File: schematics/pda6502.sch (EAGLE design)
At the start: 33 parts, among them IC1 74HC00D, IC2 74HC138D, IC3 DS1813-SMD, J1 CON_HEADER_2X07-PTH, J2 CON_HEADER_2X07-PTH, U1 W65C02S, U2 W65C22S, U3 28C256, U4 UM61256AK-12

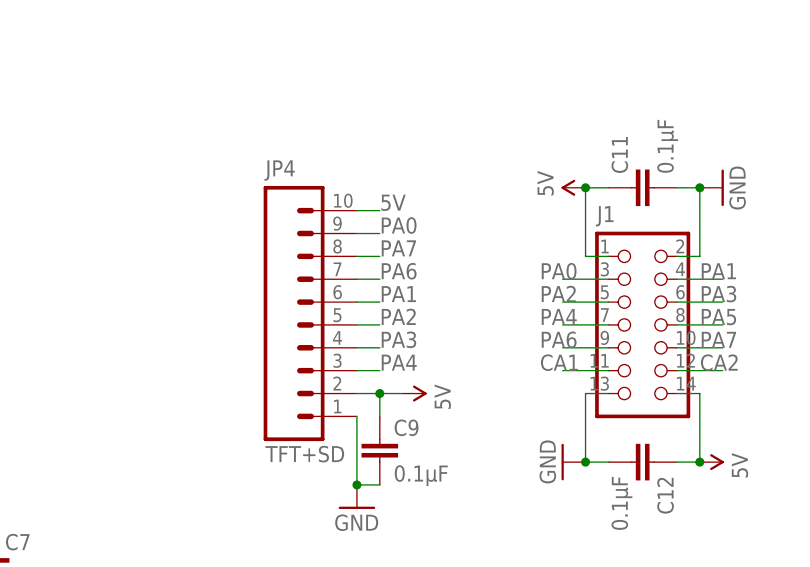
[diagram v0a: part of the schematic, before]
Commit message: schematics: TFT+SD header on PORTB for shift-register.
SR used as PWM to control backlight.
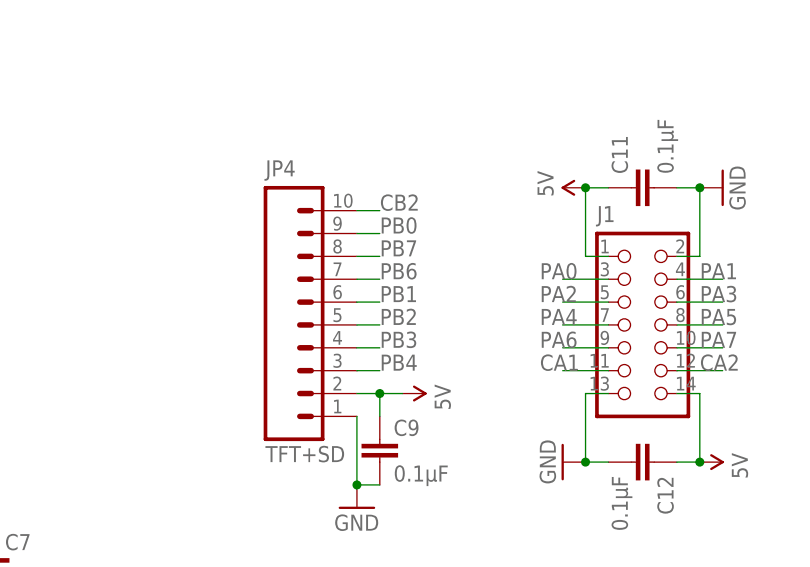
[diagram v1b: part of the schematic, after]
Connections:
- net 5V: no longer JP4.10
- net CB2: now also JP4.10
- net PA0: no longer JP4.9
- net PA1: no longer JP4.6
- net PA2: no longer JP4.5
- net PA3: no longer JP4.4
- net PA4: no longer JP4.3
- net PA6: no longer JP4.7
- net PA7: no longer JP4.8
- net PB0: now also JP4.9
- net PB1: now also JP4.6
- net PB2: now also JP4.5
- net PB3: now also JP4.4
- net PB4: now also JP4.3
- net PB6: now also JP4.7
- net PB7: now also JP4.8

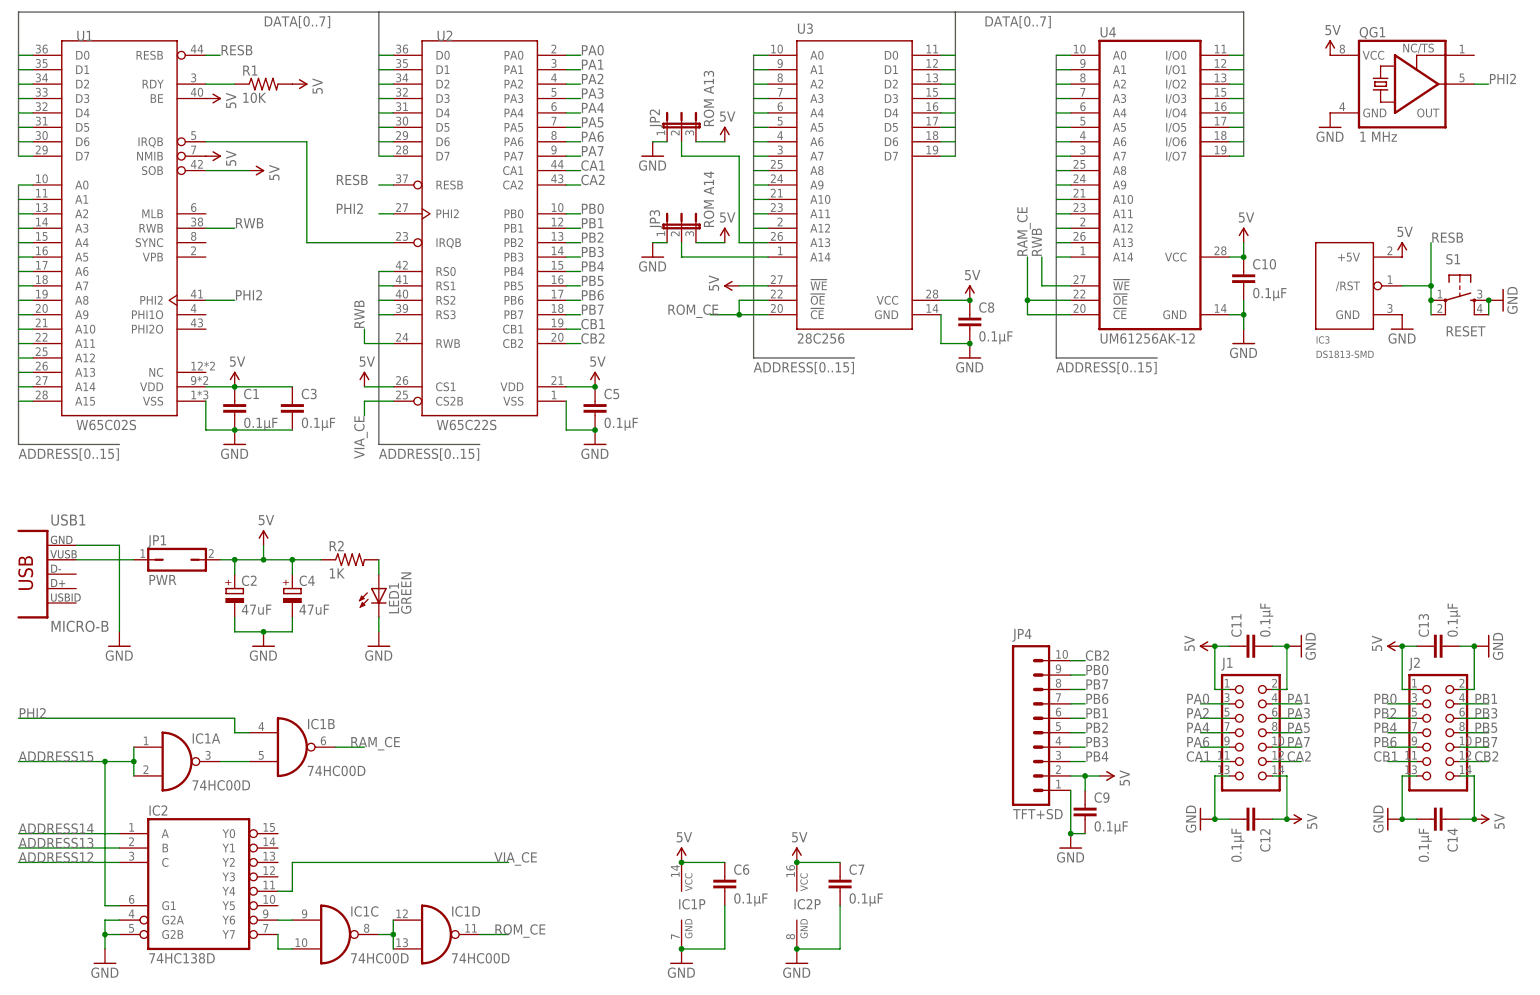
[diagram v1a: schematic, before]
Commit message: schematics: PORTB hdr changed, 40-pin hdr is back.
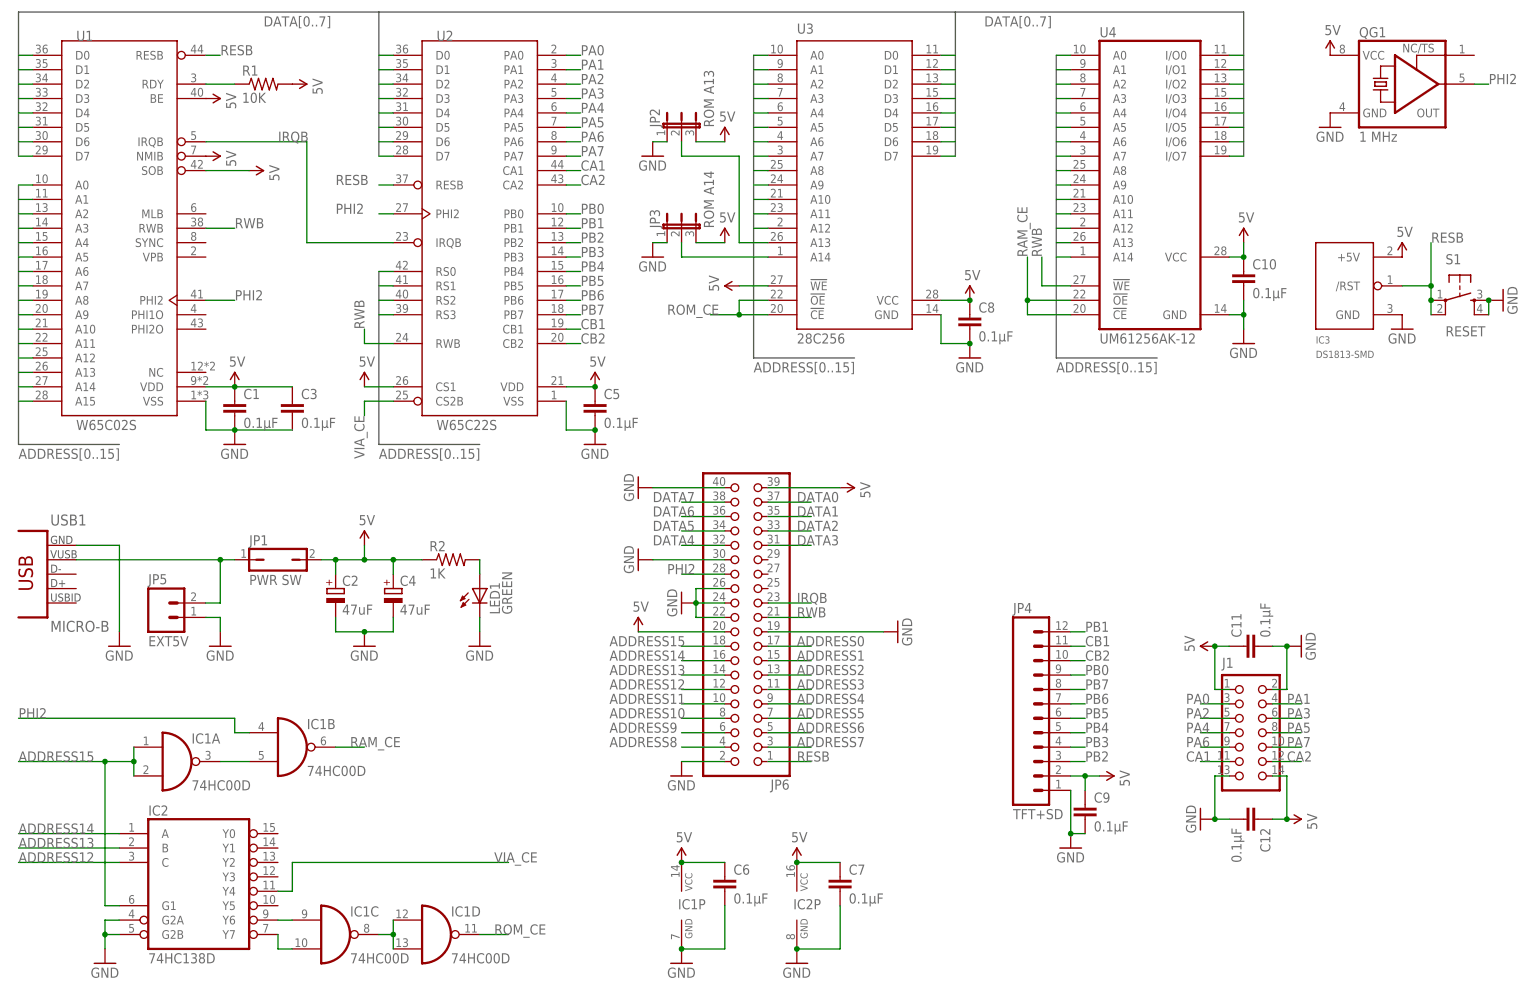
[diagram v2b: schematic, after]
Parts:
- removed C13, C14: 0.1μF, rcl:C-EUC0805
- removed J2: CON_HEADER_2X07-PTH, dangerousprototypes_devices:CON_HEADER_2X07-PTH
- added JP5: EXT5V, SparkFun-Connectors:M02PTH
- added JP6: (no value), adafruit:PINHD-2X20
- JP1: value PWR -> PWR SW
- JP4: device SparkFun-Connectors:M10" -> SparkFun-Connectors:M12PTH
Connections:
- removed net N$8: U1.IRQB, U2.IRQB
- new net IRQB: JP6.23, U1.IRQB, U2.IRQB
- net 5V: now also JP6.20, JP6.39; no longer C13.1, C14.1, J2.1, J2.14
- net ADDRESS0: now also JP6.17
- net ADDRESS1: now also JP6.15, JP6.19
- net ADDRESS10: now also JP6.8
- net ADDRESS11: now also JP6.10
- net ADDRESS12: now also JP6.12
- net ADDRESS13: now also JP6.14
- net ADDRESS14: now also JP6.16
- net ADDRESS15: now also JP6.18
- net ADDRESS2: now also JP6.13
- net ADDRESS3: now also JP6.11
- net ADDRESS4: now also JP6.9
- net ADDRESS5: now also JP6.7
- net ADDRESS6: now also JP6.5
- net ADDRESS7: now also JP6.3
- net ADDRESS8: now also JP6.4
- net ADDRESS9: now also JP6.6
- net CB1: now also JP4.11; no longer J2.11
- net CB2: no longer J2.12
- net DATA7: now also JP6.38
- net GND: now also JP5.1, JP6.2, JP6.22, JP6.24, JP6.26, JP6.30, JP6.40; no longer C13.2, C14.2, J2.13, J2.2
- net N$4: now also JP5.2
- net PB0: no longer J2.3
- net PB1: now also JP4.12; no longer J2.4, JP4.6
- net PB2: now also JP4.3; no longer J2.5, JP4.5
- net PB3: no longer J2.6
- net PB4: now also JP4.5; no longer J2.7, JP4.3
- net PB5: now also JP4.6; no longer J2.8
- net PB6: no longer J2.9
- net PB7: no longer J2.10
- net PHI2: now also JP6.28
- net RESB: now also JP6.1
- net RWB: now also JP6.21
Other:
- moved on the sheet: C2, C4, JP1, LED1, R2

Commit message: schematics: ADDRESS[0..15] renamed to ADDR[0..15] for brevity.
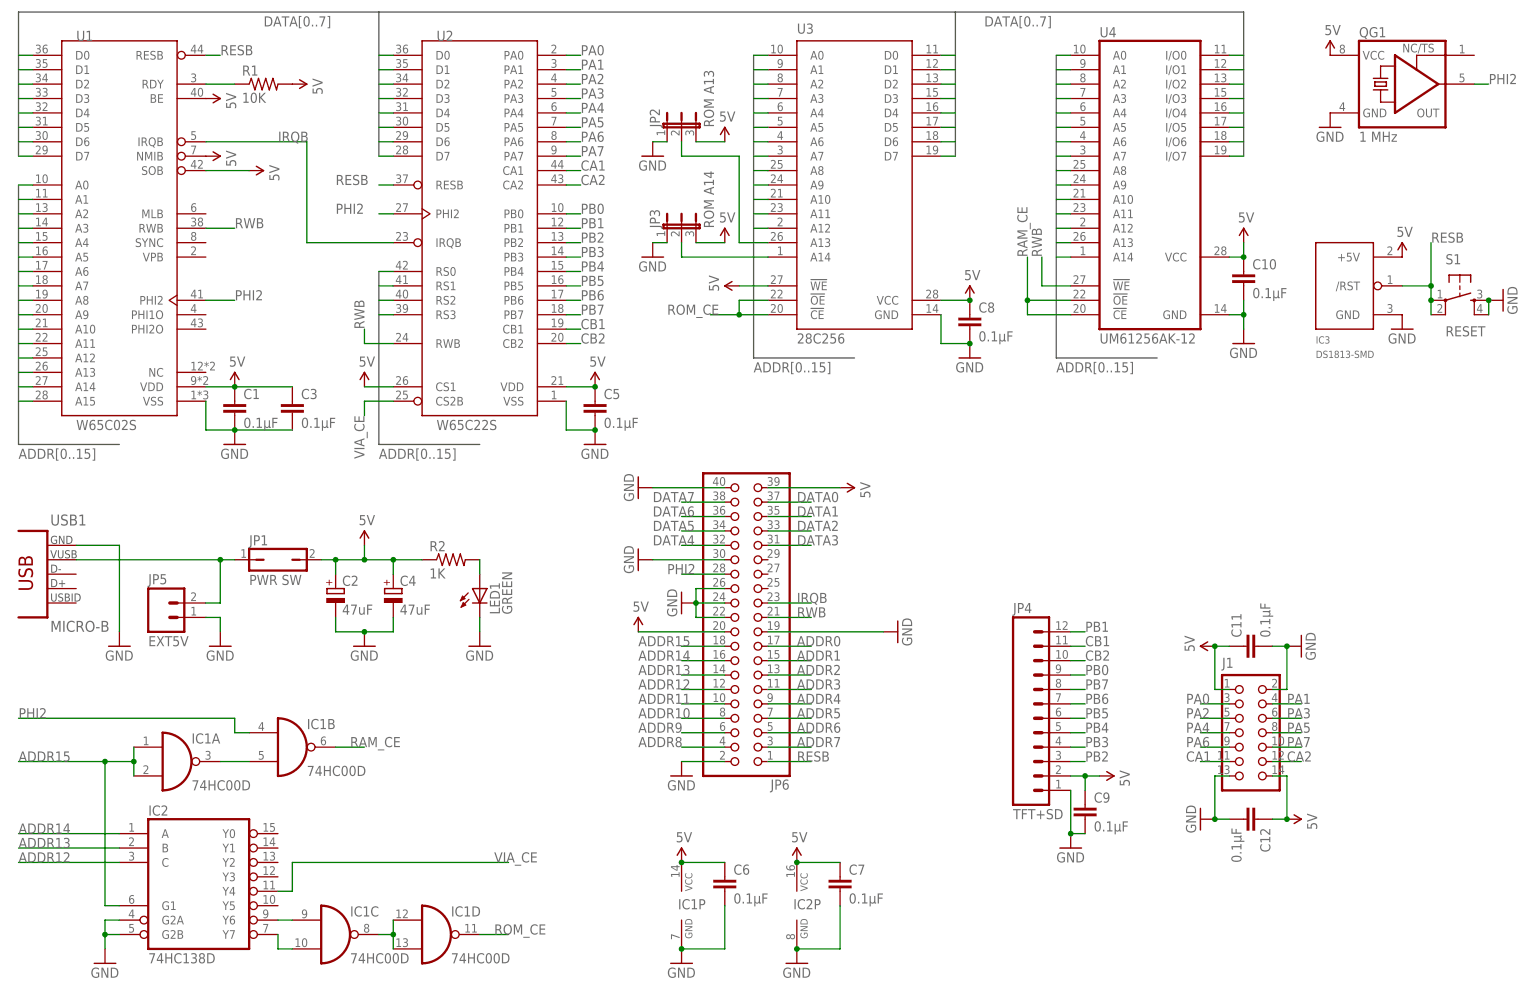
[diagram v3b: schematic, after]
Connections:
- net ADDRESS0 renamed ADDR0
- net ADDRESS1 renamed ADDR1
- net ADDRESS10 renamed ADDR10
- net ADDRESS11 renamed ADDR11
- net ADDRESS12 renamed ADDR12
- net ADDRESS13 renamed ADDR13
- net ADDRESS14 renamed ADDR14
- net ADDRESS15 renamed ADDR15
- net ADDRESS2 renamed ADDR2
- net ADDRESS3 renamed ADDR3
- net ADDRESS4 renamed ADDR4
- net ADDRESS5 renamed ADDR5
- net ADDRESS6 renamed ADDR6
- net ADDRESS7 renamed ADDR7
- net ADDRESS8 renamed ADDR8
- net ADDRESS9 renamed ADDR9
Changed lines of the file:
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@@
 </segment>
 </bus>
-<bus name="ADDRESS[0..15]">
+<bus name="ADDR[0..15]">
 <segment>
 <wire x1="5.08" y1="144.78" x2="5.08" y2="99.06" width="0.762" layer="92"/>
@@
 </segment>
 </net>
-<net name="ADDRESS0" class="0">
+<net name="ADDR0" class="0">
 <segment>
 <wire x1="5.08" y1="144.78" x2="7.62" y2="144.78" width="0.1524" layer="91"/>
@@
 </segment>
 </net>
-<net name="ADDRESS1" class="0">
+<net name="ADDR1" class="0">
 <segment>
 <wire x1="5.08" y1="142.24" x2="7.62" y2="142.24" width="0.1524" layer="91"/>
@@
 </segment>
 </net>
-<net name="ADDRESS2" class="0">
+<net name="ADDR2" class="0">
 <segment>
 <wire x1="5.08" y1="139.7" x2="7.62" y2="139.7" width="0.1524" layer="91"/>
@@
 </segment>
 </net>
-<net name="ADDRESS3" class="0">
+<net name="ADDR3" class="0">
 <segment>
 <wire x1="5.08" y1="137.16" x2="7.62" y2="137.16" width="0.1524" layer="91"/>
@@
 </segment>
 </net>
-<net name="ADDRESS4" class="0">
+<net name="ADDR4" class="0">
 <segment>
 <wire x1="5.08" y1="134.62" x2="7.62" y2="134.62" width="0.1524" layer="91"/>
@@
 </segment>
 </net>
-<net name="ADDRESS5" class="0">
+<net name="ADDR5" class="0">
 <segment>
 <wire x1="5.08" y1="132.08" x2="7.62" y2="132.08" width="0.1524" layer="91"/>
@@
 </segment>
 </net>
-<net name="ADDRESS6" class="0">
+<net name="ADDR6" class="0">
 <segment>
 <wire x1="5.08" y1="129.54" x2="7.62" y2="129.54" width="0.1524" layer="91"/>
@@
 </segment>
 </net>
-<net name="ADDRESS7" class="0">
+<net name="ADDR7" class="0">
 <segment>
 <wire x1="5.08" y1="127" x2="7.62" y2="127" width="0.1524" layer="91"/>
@@
 </segment>
 </net>
-<net name="ADDRESS8" class="0">
+<net name="ADDR8" class="0">
 <segment>
 <wire x1="5.08" y1="124.46" x2="7.62" y2="124.46" width="0.1524" layer="91"/>
@@
 <pinref part="JP6" gate="A" pin="4"/>
 <wire x1="129.54" y1="45.72" x2="121.92" y2="45.72" width="0.1524" layer="91"/>
-<label x="109.22" y="45.72" size="1.778" layer="95"/>
-</segment>
-</net>
-<net name="ADDRESS9" class="0">
+<label x="114.3" y="45.72" size="1.778" layer="95"/>
+</segment>
+</net>
+<net name="ADDR9" class="0">
 <segment>
 <wire x1="5.08" y1="121.92" x2="7.62" y2="121.92" width="0.1524" layer="91"/>
@@
 <pinref part="JP6" gate="A" pin="6"/>
 <wire x1="129.54" y1="48.26" x2="121.92" y2="48.26" width="0.1524" layer="91"/>
-<label x="109.22" y="48.26" size="1.778" layer="95"/>
-</segment>
-</net>
-<net name="ADDRESS10" class="0">
+<label x="114.3" y="48.26" size="1.778" layer="95"/>
+</segment>
+</net>
+<net name="ADDR10" class="0">
 <segment>
 <wire x1="5.08" y1="119.38" x2="7.62" y2="119.38" width="0.1524" layer="91"/>
@@
 <pinref part="JP6" gate="A" pin="8"/>
 <wire x1="129.54" y1="50.8" x2="121.92" y2="50.8" width="0.1524" layer="91"/>
-<label x="109.22" y="50.8" size="1.778" layer="95"/>
-</segment>
-</net>
-<net name="ADDRESS11" class="0">
+<label x="114.3" y="50.8" size="1.778" layer="95"/>
+</segment>
+</net>
+<net name="ADDR11" class="0">
 <segment>
 <wire x1="5.08" y1="116.84" x2="7.62" y2="116.84" width="0.1524" layer="91"/>
@@
 <pinref part="JP6" gate="A" pin="10"/>
 <wire x1="129.54" y1="53.34" x2="121.92" y2="53.34" width="0.1524" layer="91"/>
-<label x="109.22" y="53.34" size="1.778" layer="95"/>
-</segment>
-</net>
-<net name="ADDRESS12" class="0">
+<label x="114.3" y="53.34" size="1.778" layer="95"/>
+</segment>
+</net>
+<net name="ADDR12" class="0">
 <segment>
 <wire x1="5.08" y1="114.3" x2="7.62" y2="114.3" width="0.1524" layer="91"/>
@@
 <pinref part="JP6" gate="A" pin="12"/>
 <wire x1="129.54" y1="55.88" x2="121.92" y2="55.88" width="0.1524" layer="91"/>
-<label x="109.22" y="55.88" size="1.778" layer="95"/>
-</segment>
-</net>
-<net name="ADDRESS13" class="0">
+<label x="114.3" y="55.88" size="1.778" layer="95"/>
+</segment>
+</net>
+<net name="ADDR13" class="0">
 <segment>
 <wire x1="5.08" y1="111.76" x2="7.62" y2="111.76" width="0.1524" layer="91"/>
@@
 <pinref part="JP6" gate="A" pin="14"/>
 <wire x1="129.54" y1="58.42" x2="121.92" y2="58.42" width="0.1524" layer="91"/>
-<label x="109.22" y="58.42" size="1.778" layer="95"/>
-</segment>
-</net>
-<net name="ADDRESS14" class="0">
+<label x="114.3" y="58.42" size="1.778" layer="95"/>
+</segment>
+</net>
+<net name="ADDR14" class="0">
 <segment>
 <wire x1="5.08" y1="109.22" x2="7.62" y2="109.22" width="0.1524" layer="91"/>
@@
 <pinref part="JP6" gate="A" pin="16"/>
 <wire x1="129.54" y1="60.96" x2="121.92" y2="60.96" width="0.1524" layer="91"/>
-<label x="109.22" y="60.96" size="1.778" layer="95"/>
-</segment>
-</net>
-<net name="ADDRESS15" class="0">
+<label x="114.3" y="60.96" size="1.778" layer="95"/>
+</segment>
+</net>
+<net name="ADDR15" class="0">
 <segment>
 <wire x1="5.08" y1="106.68" x2="7.62" y2="106.68" width="0.1524" layer="91"/>
@@
 <pinref part="JP6" gate="A" pin="18"/>
 <wire x1="129.54" y1="63.5" x2="121.92" y2="63.5" width="0.1524" layer="91"/>
-<label x="109.22" y="63.5" size="1.778" layer="95"/>
-</segment>
-</net>
+<label x="114.3" y="63.5" size="1.778" layer="95"/>
+</segment>
+</net>
